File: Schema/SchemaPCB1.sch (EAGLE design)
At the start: 28 parts, among them J1 CON-HIROSE-COAXIAL-U.FL, J2 Programmer, U1 RN2483, U2 TPS22860DBVR, U3 ESP32, U4 SOT-89-5, U5 SI7217-B-01-IVR

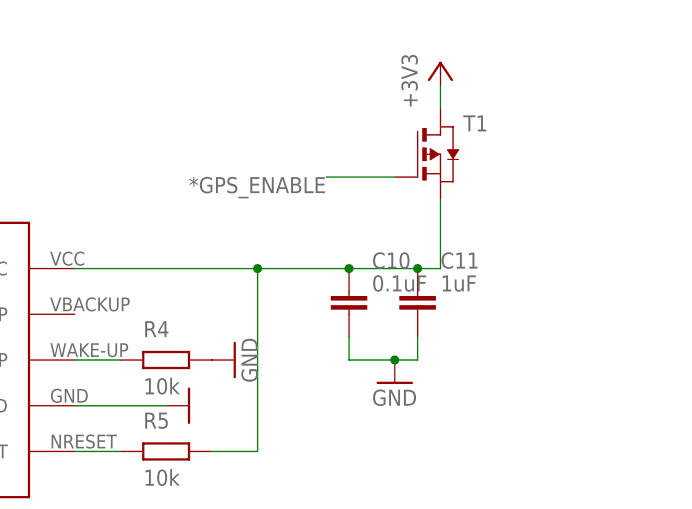
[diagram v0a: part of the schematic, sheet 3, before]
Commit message: ferrite bead toegevoegd
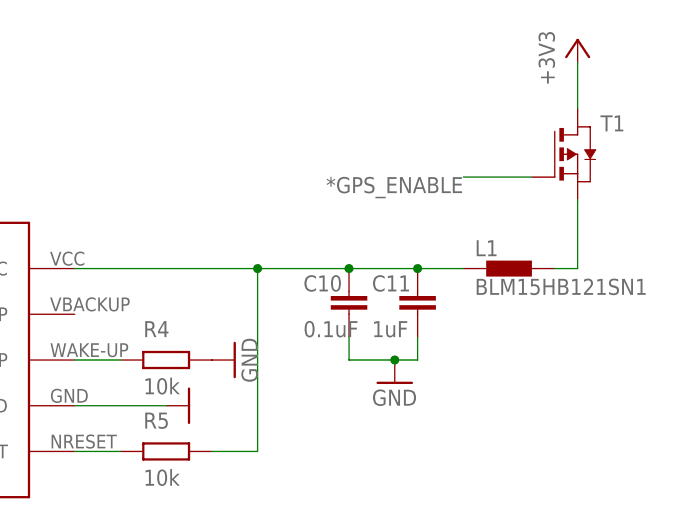
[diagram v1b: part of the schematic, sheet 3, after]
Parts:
- added L1: BLM15HB121SN1, inductors:BLM15HB121SN1
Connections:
- new net N$7: L1.2, T1.S
- net N$8: now also L1.1; no longer T1.S
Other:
- moved on the sheet: T1
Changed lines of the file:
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@@
 <part name="GND15" library="supply1" library_urn="urn:adsk.eagle:library:371" deviceset="GND" device=""/>
 <part name="U?1" library="gps" deviceset="GPS" device=""/>
+<part name="L1" library="inductors" library_urn="urn:adsk.eagle:library:243" deviceset="BLM15H" device="" package3d_urn="urn:adsk.eagle:package:15132/1" technology="B121SN1"/>
 </parts>
 <sheets>
@@
 </instance>
 <instance part="GND10" gate="1" x="144.78" y="116.84" smashed="yes" rot="R90"/>
-<instance part="+3V8" gate="G$1" x="172.72" y="154.94" smashed="yes">
-<attribute name="VALUE" x="170.18" y="149.86" size="1.778" layer="96" rot="R90"/>
-</instance>
-<instance part="T1" gate="A" x="172.72" y="144.78" smashed="yes">
-<attribute name="VALUE" x="175.26" y="144.78" size="1.778" layer="96"/>
-<attribute name="NAME" x="175.26" y="147.32" size="1.778" layer="95"/>
+<instance part="+3V8" gate="G$1" x="187.96" y="157.48" smashed="yes">
+<attribute name="VALUE" x="185.42" y="152.4" size="1.778" layer="96" rot="R90"/>
+</instance>
+<instance part="T1" gate="A" x="187.96" y="144.78" smashed="yes">
+<attribute name="VALUE" x="190.5" y="144.78" size="1.778" layer="96"/>
+<attribute name="NAME" x="190.5" y="147.32" size="1.778" layer="95"/>
 </instance>
 <instance part="R5" gate="G$1" x="142.24" y="111.76" smashed="yes">
@@
 </instance>
 <instance part="C10" gate="G$1" x="162.56" y="129.54" smashed="yes">
-<attribute name="NAME" x="165.1" y="132.08" size="1.778" layer="95"/>
-<attribute name="VALUE" x="165.1" y="129.54" size="1.778" layer="96"/>
+<attribute name="NAME" x="157.48" y="129.54" size="1.778" layer="95"/>
+<attribute name="VALUE" x="157.48" y="124.46" size="1.778" layer="96"/>
 </instance>
 <instance part="C11" gate="G$1" x="170.18" y="129.54" smashed="yes">
-<attribute name="NAME" x="172.72" y="132.08" size="1.778" layer="95"/>
-<attribute name="VALUE" x="172.72" y="129.54" size="1.778" layer="96"/>
+<attribute name="NAME" x="165.1" y="129.54" size="1.778" layer="95"/>
+<attribute name="VALUE" x="165.1" y="124.46" size="1.778" layer="96"/>
 </instance>
 <instance part="GND16" gate="1" x="167.64" y="119.38" smashed="yes">
@@
 </instance>
 <instance part="U?1" gate="G$1" x="269.24" y="114.3" smashed="yes"/>
+<instance part="L1" gate="G$1" x="180.34" y="132.08" smashed="yes">
+<attribute name="NAME" x="176.53" y="133.4516" size="1.778" layer="95"/>
+<attribute name="VALUE" x="176.53" y="129.159" size="1.778" layer="96"/>
+</instance>
 </instances>
 <busses>
@@
 <pinref part="+3V8" gate="G$1" pin="+3V3"/>
 <pinref part="T1" gate="A" pin="D"/>
-<wire x1="172.72" y1="152.4" x2="172.72" y2="149.86" width="0.1524" layer="91"/>
+<wire x1="187.96" y1="154.94" x2="187.96" y2="149.86" width="0.1524" layer="91"/>
 </segment>
 </net>
@@
 <segment>
 <pinref part="T1" gate="A" pin="G"/>
-<wire x1="167.64" y1="142.24" x2="160.02" y2="142.24" width="0.1524" layer="91"/>
-<label x="160.02" y="142.24" size="1.778" layer="95" rot="R180"/>
+<wire x1="182.88" y1="142.24" x2="175.26" y2="142.24" width="0.1524" layer="91"/>
+<label x="175.26" y="142.24" size="1.778" layer="95" rot="R180"/>
 </segment>
 </net>
@@
 <wire x1="147.32" y1="111.76" x2="152.4" y2="111.76" width="0.1524" layer="91"/>
 <wire x1="132.08" y1="132.08" x2="152.4" y2="132.08" width="0.1524" layer="91"/>
-<pinref part="T1" gate="A" pin="S"/>
-<wire x1="172.72" y1="139.7" x2="172.72" y2="132.08" width="0.1524" layer="91"/>
-<wire x1="172.72" y1="132.08" x2="170.18" y2="132.08" width="0.1524" layer="91"/>
 <junction x="152.4" y="132.08"/>
 <pinref part="C10" gate="G$1" pin="1"/>
@@
 <junction x="170.18" y="132.08"/>
 <pinref part="U?1" gate="G$1" pin="VCC"/>
+<pinref part="L1" gate="G$1" pin="1"/>
+<wire x1="175.26" y1="132.08" x2="170.18" y2="132.08" width="0.1524" layer="91"/>
 </segment>
 </net>
@@
 </segment>
 </net>
+<net name="N$7" class="0">
+<segment>
+<pinref part="T1" gate="A" pin="S"/>
+<wire x1="187.96" y1="139.7" x2="187.96" y2="132.08" width="0.1524" layer="91"/>
+<pinref part="L1" gate="G$1" pin="2"/>
+<wire x1="187.96" y1="132.08" x2="185.42" y2="132.08" width="0.1524" layer="91"/>
+</segment>
+</net>

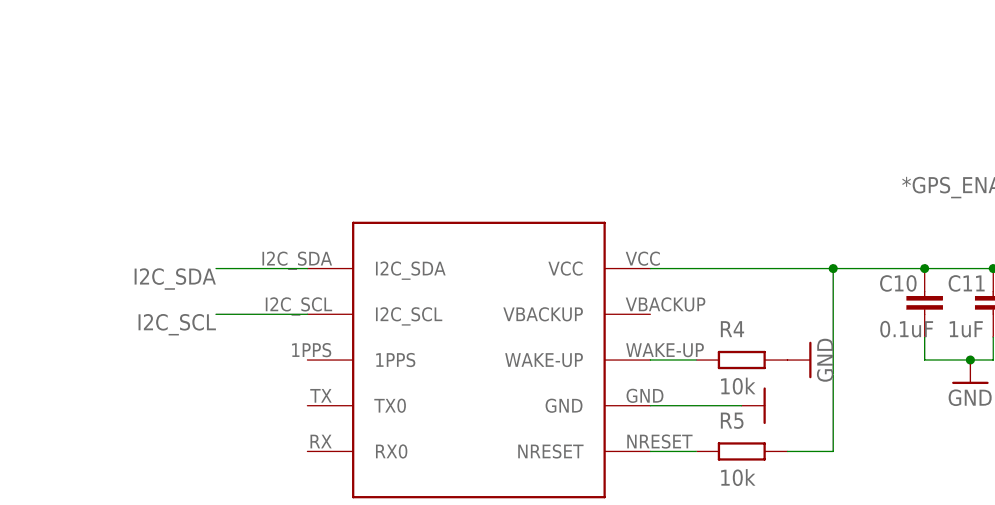
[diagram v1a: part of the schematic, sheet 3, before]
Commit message: pull-up toegevoegd op I2C gps
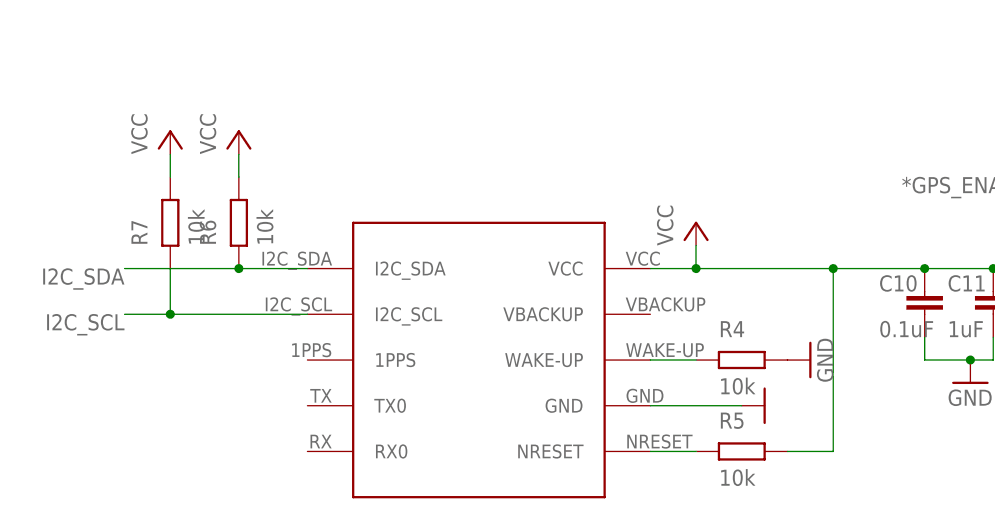
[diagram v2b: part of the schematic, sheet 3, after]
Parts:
- added R6, R7: 10k, ngspice-simulation:R
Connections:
- removed net N$8: C10.1, C11.1, L1.1, R5.2, U?1.VCC
- new net VCC: C10.1, C11.1, L1.1, R5.2, R6.2, R7.2, U?1.VCC
- net I2C_SCL: now also R7.1
- net I2C_SDA: now also R6.1
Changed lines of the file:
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@@
 <part name="U?1" library="gps" deviceset="GPS" device=""/>
 <part name="L1" library="inductors" library_urn="urn:adsk.eagle:library:243" deviceset="BLM15H" device="" package3d_urn="urn:adsk.eagle:package:15132/1" technology="B121SN1"/>
+<part name="R6" library="ngspice-simulation" library_urn="urn:adsk.eagle:library:527439" deviceset="R" device="" value="10k"/>
+<part name="R7" library="ngspice-simulation" library_urn="urn:adsk.eagle:library:527439" deviceset="R" device="" value="10k"/>
+<part name="P+1" library="supply1" library_urn="urn:adsk.eagle:library:371" deviceset="VCC" device=""/>
+<part name="P+2" library="supply1" library_urn="urn:adsk.eagle:library:371" deviceset="VCC" device=""/>
+<part name="P+3" library="supply1" library_urn="urn:adsk.eagle:library:371" deviceset="VCC" device=""/>
 </parts>
 <sheets>
@@
 <attribute name="VALUE" x="176.53" y="129.159" size="1.778" layer="96"/>
 </instance>
+<instance part="R6" gate="G$1" x="86.36" y="137.16" smashed="yes" rot="R90">
+<attribute name="NAME" x="83.82" y="134.62" size="1.778" layer="95" rot="R90"/>
+<attribute name="VALUE" x="90.17" y="134.62" size="1.778" layer="96" rot="R90"/>
+</instance>
+<instance part="R7" gate="G$1" x="78.74" y="137.16" smashed="yes" rot="R90">
+<attribute name="NAME" x="76.2" y="134.62" size="1.778" layer="95" rot="R90"/>
+<attribute name="VALUE" x="82.55" y="134.62" size="1.778" layer="96" rot="R90"/>
+</instance>
+<instance part="P+1" gate="VCC" x="137.16" y="137.16" smashed="yes">
+<attribute name="VALUE" x="134.62" y="134.62" size="1.778" layer="96" rot="R90"/>
+</instance>
+<instance part="P+2" gate="VCC" x="78.74" y="147.32" smashed="yes">
+<attribute name="VALUE" x="76.2" y="144.78" size="1.778" layer="96" rot="R90"/>
+</instance>
+<instance part="P+3" gate="VCC" x="86.36" y="147.32" smashed="yes">
+<attribute name="VALUE" x="83.82" y="144.78" size="1.778" layer="96" rot="R90"/>
+</instance>
 </instances>
 <busses>
@@
 <net name="I2C_SDA" class="0">
 <segment>
-<wire x1="93.98" y1="132.08" x2="83.82" y2="132.08" width="0.1524" layer="91"/>
-<label x="83.82" y="132.08" size="1.778" layer="95" rot="R180"/>
+<wire x1="93.98" y1="132.08" x2="86.36" y2="132.08" width="0.1524" layer="91"/>
+<label x="73.66" y="132.08" size="1.778" layer="95" rot="R180"/>
 <pinref part="U?1" gate="G$1" pin="I2C_SDA"/>
+<pinref part="R6" gate="G$1" pin="1"/>
+<junction x="86.36" y="132.08"/>
+<wire x1="86.36" y1="132.08" x2="73.66" y2="132.08" width="0.1524" layer="91"/>
 </segment>
 </net>
 <net name="I2C_SCL" class="0">
 <segment>
-<wire x1="93.98" y1="127" x2="83.82" y2="127" width="0.1524" layer="91"/>
-<label x="83.82" y="127" size="1.778" layer="95" rot="R180"/>
+<wire x1="93.98" y1="127" x2="78.74" y2="127" width="0.1524" layer="91"/>
+<label x="73.66" y="127" size="1.778" layer="95" rot="R180"/>
 <pinref part="U?1" gate="G$1" pin="I2C_SCL"/>
+<pinref part="R7" gate="G$1" pin="1"/>
+<wire x1="78.74" y1="132.08" x2="78.74" y2="127" width="0.1524" layer="91"/>
+<wire x1="78.74" y1="127" x2="73.66" y2="127" width="0.1524" layer="91"/>
+<junction x="78.74" y="127"/>
 </segment>
 </net>
@@
 </segment>
 </net>
-<net name="N$8" class="0">
+<net name="N$5" class="0">
+<segment>
+<pinref part="R4" gate="G$1" pin="1"/>
+<wire x1="132.08" y1="121.92" x2="137.16" y2="121.92" width="0.1524" layer="91"/>
+<pinref part="U?1" gate="G$1" pin="WAKE-UP"/>
+</segment>
+</net>
+<net name="N$7" class="0">
+<segment>
+<pinref part="T1" gate="A" pin="S"/>
+<wire x1="187.96" y1="139.7" x2="187.96" y2="132.08" width="0.1524" layer="91"/>
+<pinref part="L1" gate="G$1" pin="2"/>
+<wire x1="187.96" y1="132.08" x2="185.42" y2="132.08" width="0.1524" layer="91"/>
+</segment>
+</net>
+<net name="VCC" class="0">
 <segment>
 <wire x1="152.4" y1="132.08" x2="152.4" y2="111.76" width="0.1524" layer="91"/>
 <pinref part="R5" gate="G$1" pin="2"/>
 <wire x1="147.32" y1="111.76" x2="152.4" y2="111.76" width="0.1524" layer="91"/>
-<wire x1="132.08" y1="132.08" x2="152.4" y2="132.08" width="0.1524" layer="91"/>
+<wire x1="132.08" y1="132.08" x2="137.16" y2="132.08" width="0.1524" layer="91"/>
 <junction x="152.4" y="132.08"/>
 <pinref part="C10" gate="G$1" pin="1"/>
+<wire x1="137.16" y1="132.08" x2="152.4" y2="132.08" width="0.1524" layer="91"/>
 <wire x1="170.18" y1="132.08" x2="162.56" y2="132.08" width="0.1524" layer="91"/>
 <wire x1="162.56" y1="132.08" x2="152.4" y2="132.08" width="0.1524" layer="91"/>
@@
 <pinref part="L1" gate="G$1" pin="1"/>
 <wire x1="175.26" y1="132.08" x2="170.18" y2="132.08" width="0.1524" layer="91"/>
-</segment>
-</net>
-<net name="N$5" class="0">
-<segment>
-<pinref part="R4" gate="G$1" pin="1"/>
-<wire x1="132.08" y1="121.92" x2="137.16" y2="121.92" width="0.1524" layer="91"/>
-<pinref part="U?1" gate="G$1" pin="WAKE-UP"/>
-</segment>
-</net>
-<net name="N$7" class="0">
-<segment>
-<pinref part="T1" gate="A" pin="S"/>
-<wire x1="187.96" y1="139.7" x2="187.96" y2="132.08" width="0.1524" layer="91"/>
-<pinref part="L1" gate="G$1" pin="2"/>
-<wire x1="187.96" y1="132.08" x2="185.42" y2="132.08" width="0.1524" layer="91"/>
-</segment>
-</net>
+<pinref part="P+1" gate="VCC" pin="VCC"/>
+<wire x1="137.16" y1="134.62" x2="137.16" y2="132.08" width="0.1524" layer="91"/>
+<junction x="137.16" y="132.08"/>
+</segment>
+<segment>
+<pinref part="R7" gate="G$1" pin="2"/>
+<wire x1="78.74" y1="142.24" x2="78.74" y2="144.78" width="0.1524" layer="91"/>
+<pinref part="P+2" gate="VCC" pin="VCC"/>
+</segment>
+<segment>
+<pinref part="R6" gate="G$1" pin="2"/>
+<wire x1="86.36" y1="144.78" x2="86.36" y2="142.24" width="0.1524" layer="91"/>
+<pinref part="P+3" gate="VCC" pin="VCC"/>
+</segment>
+</net>

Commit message: gps schema aangepast
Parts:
- added R8: 10k, ngspice-simulation:R
- T1: value (none) -> SiSH615ADN
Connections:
- net *GPS_ENABLE: now also R8.1, R8.2
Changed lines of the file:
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@@
 <part name="GND10" library="supply1" library_urn="urn:adsk.eagle:library:371" deviceset="GND" device=""/>
 <part name="+3V8" library="supply1" library_urn="urn:adsk.eagle:library:371" deviceset="+3V3" device=""/>
-<part name="T1" library="zetex" library_urn="urn:adsk.eagle:library:418" deviceset="PMOSSOT23" device="" package3d_urn="urn:adsk.eagle:package:30981/1"/>
+<part name="T1" library="zetex" library_urn="urn:adsk.eagle:library:418" deviceset="PMOSSOT23" device="" package3d_urn="urn:adsk.eagle:package:30981/1" value="SiSH615ADN"/>
 <part name="R5" library="ngspice-simulation" library_urn="urn:adsk.eagle:library:527439" deviceset="R" device="" value="10k"/>
 <part name="C10" library="ngspice-simulation" library_urn="urn:adsk.eagle:library:527439" deviceset="C" device="" value="0.1uF"/>
@@
 <part name="P+2" library="supply1" library_urn="urn:adsk.eagle:library:371" deviceset="VCC" device=""/>
 <part name="P+3" library="supply1" library_urn="urn:adsk.eagle:library:371" deviceset="VCC" device=""/>
+<part name="R8" library="ngspice-simulation" library_urn="urn:adsk.eagle:library:527439" deviceset="R" device="" value="10k"/>
 </parts>
 <sheets>
@@
 <attribute name="VALUE" x="83.82" y="144.78" size="1.778" layer="96" rot="R90"/>
 </instance>
+<instance part="R8" gate="G$1" x="170.18" y="142.24" smashed="yes">
+<attribute name="NAME" x="167.64" y="144.78" size="1.778" layer="95"/>
+<attribute name="VALUE" x="167.64" y="138.43" size="1.778" layer="96"/>
+</instance>
 </instances>
 <busses>
@@
 <segment>
 <wire x1="93.98" y1="132.08" x2="86.36" y2="132.08" width="0.1524" layer="91"/>
-<label x="73.66" y="132.08" size="1.778" layer="95" rot="R180"/>
+<label x="81.28" y="132.08" size="1.778" layer="95" rot="R180"/>
 <pinref part="U?1" gate="G$1" pin="I2C_SDA"/>
 <pinref part="R6" gate="G$1" pin="1"/>
 <junction x="86.36" y="132.08"/>
-<wire x1="86.36" y1="132.08" x2="73.66" y2="132.08" width="0.1524" layer="91"/>
+<wire x1="86.36" y1="132.08" x2="81.28" y2="132.08" width="0.1524" layer="91"/>
 </segment>
 </net>
@@
 <pinref part="T1" gate="A" pin="G"/>
 <wire x1="182.88" y1="142.24" x2="175.26" y2="142.24" width="0.1524" layer="91"/>
-<label x="175.26" y="142.24" size="1.778" layer="95" rot="R180"/>
-</segment>
-</net>
+<pinref part="R8" gate="G$1" pin="2"/>
+</segment>
+<segment>
+<pinref part="R8" gate="G$1" pin="1"/>
+<wire x1="165.1" y1="142.24" x2="162.56" y2="142.24" width="0.1524" layer="91"/>
+<label x="162.56" y="142.24" size="1.778" layer="95" rot="R180"/>
+</segment>
+</net>

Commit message: Bezig aan board
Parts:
- removed C11: 1uF, ngspice-simulation:C
- removed R2, R3: 4k6Û, --CoolTeamLib:R-EU_0805M0805
- added C12: (no value), rcl:C-EUC0805
- C10: value 0.1uF -> (none); device ngspice-simulation:C -> rcl:C-EUC0805
- R4, R5, R6, R7, R8: value 10k -> (none); device ngspice-simulation:R -> rcl:R-EU_R0805
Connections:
- removed net VCC: C10.1, C11.1, L1.1, R5.2, R6.2, R7.2, U?1.VCC
- new net GPS_ENABLE: R8.1
- new net N$8: C10.1, C12.1, L1.1, R5.2, U?1.VCC
- net *GPS_ENABLE: no longer R8.1
- net +3V3: now also R6.2, R7.2; no longer R2.2, R3.2
- net GND: now also C12.2; no longer C11.2
- net I2C_SCL: now also R6.1; no longer R2.1, R7.1
- net I2C_SDA: now also R7.1; no longer R3.1, R6.1
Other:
- moved on the sheet: C10, R6, R7

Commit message: mosfet symbool en footprint aangepast
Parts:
- removed T1: SiSH615ADN, zetex:PMOSSOT23
- added Q?1: PMOS, gps:PMOS
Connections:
- net *GPS_ENABLE: now also Q?1.G; no longer T1.G
- net +3V3: now also Q?1.S1, Q?1.S2, Q?1.S3; no longer T1.D
- net N$7: now also Q?1.D1, Q?1.D2, Q?1.D3, Q?1.D4; no longer T1.S
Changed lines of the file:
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@@
 <part name="GND10" library="supply1" library_urn="urn:adsk.eagle:library:371" deviceset="GND" device=""/>
 <part name="+3V8" library="supply1" library_urn="urn:adsk.eagle:library:371" deviceset="+3V3" device=""/>
-<part name="T1" library="zetex" library_urn="urn:adsk.eagle:library:418" deviceset="PMOSSOT23" device="" package3d_urn="urn:adsk.eagle:package:30981/1" value="SiSH615ADN"/>
 <part name="GND16" library="supply1" library_urn="urn:adsk.eagle:library:371" deviceset="GND" device=""/>
 <part name="GND15" library="supply1" library_urn="urn:adsk.eagle:library:371" deviceset="GND" device=""/>
@@
 <part name="+3V9" library="supply1" library_urn="urn:adsk.eagle:library:371" deviceset="+3V3" device=""/>
 <part name="+3V10" library="supply1" library_urn="urn:adsk.eagle:library:371" deviceset="+3V3" device=""/>
+<part name="Q?1" library="gps" deviceset="PMOS" device=""/>
 </parts>
 <sheets>
@@
 </instance>
 <instance part="GND10" gate="1" x="144.78" y="116.84" smashed="yes" rot="R90"/>
-<instance part="+3V8" gate="G$1" x="187.96" y="157.48" smashed="yes">
-<attribute name="VALUE" x="185.42" y="152.4" size="1.778" layer="96" rot="R90"/>
-</instance>
-<instance part="T1" gate="A" x="187.96" y="144.78" smashed="yes">
-<attribute name="VALUE" x="190.5" y="144.78" size="1.778" layer="96"/>
-<attribute name="NAME" x="190.5" y="147.32" size="1.778" layer="95"/>
+<instance part="+3V8" gate="G$1" x="182.88" y="154.94" smashed="yes">
+<attribute name="VALUE" x="180.34" y="149.86" size="1.778" layer="96" rot="R90"/>
 </instance>
 <instance part="GND16" gate="1" x="167.64" y="119.38" smashed="yes">
@@
 <attribute name="VALUE" x="83.82" y="142.24" size="1.778" layer="96" rot="R90"/>
 </instance>
+<instance part="Q?1" gate="G$1" x="193.802" y="146.2405" smashed="yes"/>
 </instances>
 <busses>
@@
 <net name="+3V3" class="0">
 <segment>
-<pinref part="+3V8" gate="G$1" pin="+3V3"/>
-<pinref part="T1" gate="A" pin="D"/>
-<wire x1="187.96" y1="154.94" x2="187.96" y2="149.86" width="0.1524" layer="91"/>
-</segment>
-<segment>
 <wire x1="78.74" y1="142.24" x2="78.74" y2="144.78" width="0.1524" layer="91"/>
 <pinref part="R6" gate="G$1" pin="2"/>
@@
 <pinref part="+3V10" gate="G$1" pin="+3V3"/>
 </segment>
+<segment>
+<pinref part="Q?1" gate="G$1" pin="S3"/>
+<pinref part="+3V8" gate="G$1" pin="+3V3"/>
+<wire x1="186.802" y1="144.2405" x2="182.88" y2="144.2405" width="0.1524" layer="91"/>
+<wire x1="182.88" y1="144.2405" x2="182.88" y2="146.2405" width="0.1524" layer="91"/>
+<pinref part="Q?1" gate="G$1" pin="S2"/>
+<wire x1="182.88" y1="146.2405" x2="182.88" y2="148.2405" width="0.1524" layer="91"/>
+<wire x1="182.88" y1="149.86" x2="182.88" y2="152.4" width="0.1524" layer="91"/>
+<wire x1="186.802" y1="146.2405" x2="182.88" y2="146.2405" width="0.1524" layer="91"/>
+<pinref part="Q?1" gate="G$1" pin="S1"/>
+<wire x1="186.802" y1="148.2405" x2="182.88" y2="148.2405" width="0.1524" layer="91"/>
+<wire x1="182.88" y1="148.2405" x2="182.88" y2="149.86" width="0.1524" layer="91"/>
+</segment>
 </net>
 <net name="*GPS_ENABLE" class="0">
 <segment>
-<pinref part="T1" gate="A" pin="G"/>
-<wire x1="182.88" y1="142.24" x2="175.26" y2="142.24" width="0.1524" layer="91"/>
+<wire x1="186.802" y1="142.24" x2="175.26" y2="142.24" width="0.1524" layer="91"/>
 <pinref part="R8" gate="G$1" pin="2"/>
+<pinref part="Q?1" gate="G$1" pin="G"/>
+<wire x1="186.802" y1="142.24" x2="186.802" y2="142.2405" width="0.1524" layer="91"/>
 </segment>
 </net>
@@
 <net name="N$7" class="0">
 <segment>
-<pinref part="T1" gate="A" pin="S"/>
-<wire x1="187.96" y1="139.7" x2="187.96" y2="132.08" width="0.1524" layer="91"/>
 <pinref part="L1" gate="G$1" pin="2"/>
-<wire x1="187.96" y1="132.08" x2="185.42" y2="132.08" width="0.1524" layer="91"/>
-</segment>
-</net>
+<pinref part="Q?1" gate="G$1" pin="D4"/>
+<wire x1="209.802" y1="148.2405" x2="215.9" y2="148.2405" width="0.1524" layer="91"/>
+<wire x1="215.9" y1="148.2405" x2="215.9" y2="146.304" width="0.1524" layer="91"/>
+<wire x1="215.9" y1="146.304" x2="215.9" y2="146.2405" width="0.1524" layer="91"/>
+<wire x1="215.9" y1="142.24" x2="215.9" y2="132.08" width="0.1524" layer="91"/>
+<wire x1="215.9" y1="132.08" x2="185.42" y2="132.08" width="0.1524" layer="91"/>
+<pinref part="Q?1" gate="G$1" pin="D3"/>
+<wire x1="209.802" y1="146.2405" x2="215.9" y2="146.2405" width="0.1524" layer="91"/>
+<wire x1="215.9" y1="146.2405" x2="215.9" y2="144.272" width="0.1524" layer="91"/>
+<pinref part="Q?1" gate="G$1" pin="D2"/>
+<wire x1="215.9" y1="144.272" x2="215.9" y2="144.2405" width="0.1524" layer="91"/>
+<wire x1="209.802" y1="144.2405" x2="215.9" y2="144.2405" width="0.1524" layer="91"/>
+<pinref part="Q?1" gate="G$1" pin="D1"/>
+<wire x1="215.9" y1="144.2405" x2="215.9" y2="142.24" width="0.1524" layer="91"/>
+<wire x1="209.802" y1="142.2405" x2="209.802" y2="142.24" width="0.1524" layer="91"/>
+<wire x1="209.802" y1="142.24" x2="215.9" y2="142.24" width="0.1524" layer="91"/>
+<junction x="215.9" y="142.24"/>
+<junction x="215.9" y="146.304"/>
+<junction x="215.9" y="144.272"/>
+</segment>
+</net>
